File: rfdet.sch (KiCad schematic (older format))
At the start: 8 parts, among them Q1 MMBT6427

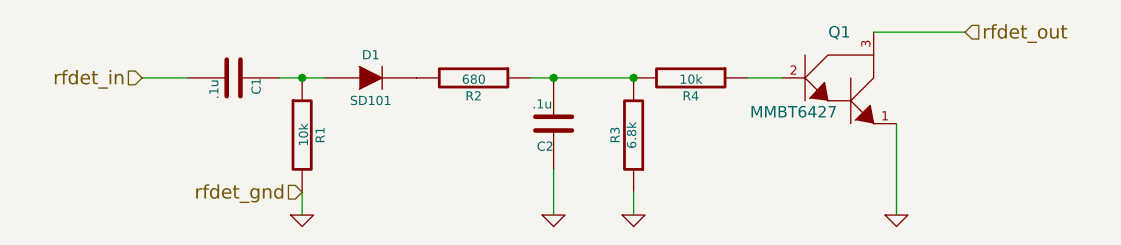
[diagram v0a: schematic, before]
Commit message: Fixes #2: Q1 pads did not match
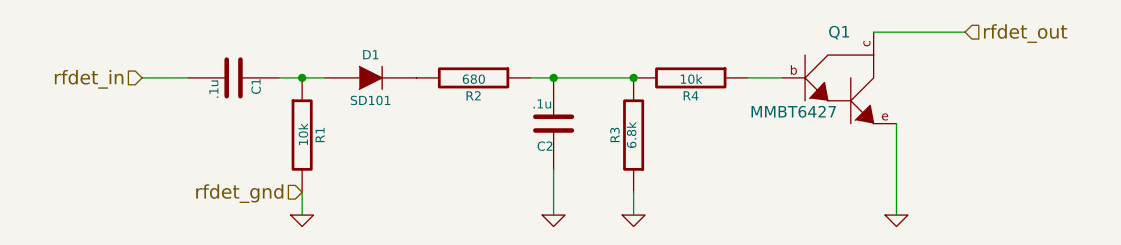
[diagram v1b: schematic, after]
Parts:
- removed Q1: MMBT6427, Transistors_SMD:sot23, symbol DARL_N
- added Q1: MMBT6427, symbol NU9J_DARL_N
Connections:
- net GND: now also Q1.e
- net rfdet_out: now also Q1.c
- net at R4.1: now also Q1.b
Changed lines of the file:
@@
 LIBS:transformers
 LIBS:relays
+LIBS:nu9j-transistors
 LIBS:qrpamp-cache
 EELAYER 25 0
@@
 Wire Wire Line
 	4100 3700 3900 3700
-$Comp
-L DARL_N Q1
-U 1 1 5470D157
-P 6950 3750
-F 0 "Q1" H 6950 4000 50  0000 C CNN
-F 1 "MMBT6427" H 6750 3650 50  0000 C CNN
-F 2 "Transistors_SMD:sot23" H 6950 3750 60  0001 C CNN
-F 3 "" H 6950 3750 60  0000 C CNN
-	1    6950 3750
-	1    0    0    -1
-$EndComp
 Wire Wire Line
 	5600 3700 6050 3700
@@
 	-1   0    0    1
 $EndComp
+$Comp
+L NU9J_DARL_N Q1
+U 1 1 54FC9320
+P 6950 3750
+F 0 "Q1" H 6950 4000 50  0000 C CNN
+F 1 "MMBT6427" H 6750 3650 50  0000 C CNN
+F 2 "" H 6950 3750 60  0000 C CNN
+F 3 "" H 6950 3750 60  0000 C CNN
+	1    6950 3750
+	1    0    0    -1
+$EndComp
 $EndSCHEMATC

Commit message: Schematic changes to go with #3 (extending sot23 pads)
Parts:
- Q1: footprint (none) -> nu9j-footprints:SOT-23-EBC_HandSoldering
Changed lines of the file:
@@
 F 0 "Q1" H 6950 4000 50  0000 C CNN
 F 1 "MMBT6427" H 6750 3650 50  0000 C CNN
-F 2 "" H 6950 3750 60  0000 C CNN
+F 2 "nu9j-footprints:SOT-23-EBC_HandSoldering" H 6950 3750 60  0001 C CNN
 F 3 "" H 6950 3750 60  0000 C CNN
 	1    6950 3750
